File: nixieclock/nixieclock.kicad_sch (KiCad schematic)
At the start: 0 parts

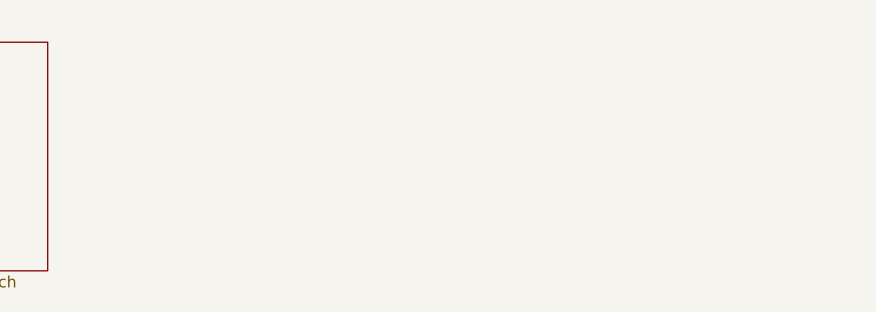
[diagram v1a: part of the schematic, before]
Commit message: added nixie breakout, began shift registers
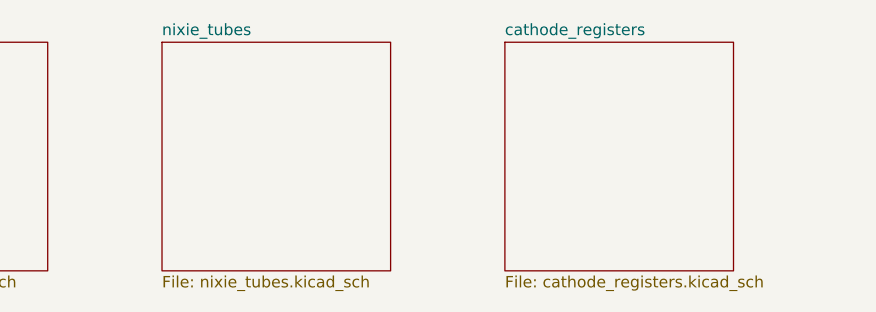
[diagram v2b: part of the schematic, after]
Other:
- added sheet cathode_registers (cathode_registers.kicad_sch)
- added sheet nixie_tubes (nixie_tubes.kicad_sch)
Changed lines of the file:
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@@
 (kicad_sch (version 20200828) (generator eeschema)
-  (page 1 2)
+  (page 1 4)
   (paper "A4")
   (title_block
     (title "Nixie Clock")
-    (date "2021-03-08")
+    (date "2021-03-10")
     (company "Bastian de Byl")
+  )
+  (sheet (at 101.6 25.4) (size 25.4 25.4)
+    (stroke (width 0.001) (type solid) (color 132 0 132 1))
+    (fill (color 255 255 255 0.0000))
+    (property "Sheet name" "cathode_registers" (id 0) (at 101.6 24.7641 0)
+      (effects (font (size 1.27 1.27)) (justify left bottom))
+    )
+    (property "Sheet file" "cathode_registers.kicad_sch" (id 1) (at 101.6 51.3089 0)
+      (effects (font (size 1.27 1.27)) (justify left top))
+    )
   )
   (sheet (at 25.4 25.4) (size 25.4 25.4)
@@
     )
     (property "Sheet file" "hv_supply.kicad_sch" (id 1) (at 25.4 51.3089 0)
+      (effects (font (size 1.27 1.27)) (justify left top))
+    )
+  )
+  (sheet (at 63.5 25.4) (size 25.4 25.4)
+    (stroke (width 0.001) (type solid) (color 132 0 132 1))
+    (fill (color 255 255 255 0.0000))
+    (property "Sheet name" "nixie_tubes" (id 0) (at 63.5 24.7641 0)
+      (effects (font (size 1.27 1.27)) (justify left bottom))
+    )
+    (property "Sheet file" "nixie_tubes.kicad_sch" (id 1) (at 63.5 51.3089 0)
       (effects (font (size 1.27 1.27)) (justify left top))
     )
@@
       (reference "U1") (unit 1) (value "LT3757AEMSE") (footprint "Package_SO:MSOP-10-1EP_3x3mm_P0.5mm_EP1.68x1.88mm")
     )
+    (path "/a46896f1-3299-462b-8eac-566ddac50b81/c7103b38-a6f4-42d2-a022-37c0fb310621"
+      (reference "R9") (unit 1) (value "R") (footprint "Resistor_SMD:R_0805_2012Metric_Pad1.15x1.40mm_HandSolder")
+    )
+    (path "/a46896f1-3299-462b-8eac-566ddac50b81/962332e7-a564-4eee-ba04-af4a2363d1a7"
+      (reference "R10") (unit 1) (value "R") (footprint "Resistor_SMD:R_0805_2012Metric_Pad1.15x1.40mm_HandSolder")
+    )
+    (path "/a46896f1-3299-462b-8eac-566ddac50b81/3cb47c1b-a308-4405-ab12-750a289a57fe"
+      (reference "R11") (unit 1) (value "R") (footprint "Resistor_SMD:R_0805_2012Metric_Pad1.15x1.40mm_HandSolder")
+    )
+    (path "/a46896f1-3299-462b-8eac-566ddac50b81/31d7a4f6-bd29-4607-8fc2-1aea2457c99a"
+      (reference "R12") (unit 1) (value "R") (footprint "Resistor_SMD:R_0805_2012Metric_Pad1.15x1.40mm_HandSolder")
+    )
+    (path "/a46896f1-3299-462b-8eac-566ddac50b81/55bc21e7-2697-464a-a01c-38e1e7b3f773"
+      (reference "R13") (unit 1) (value "R") (footprint "Resistor_SMD:R_0805_2012Metric_Pad1.15x1.40mm_HandSolder")
+    )
+    (path "/a46896f1-3299-462b-8eac-566ddac50b81/c23b582a-658a-4b65-9c96-b9e08b0bf0cc"
+      (reference "R14") (unit 1) (value "R") (footprint "Resistor_SMD:R_0805_2012Metric_Pad1.15x1.40mm_HandSolder")
+    )
+    (path "/a46896f1-3299-462b-8eac-566ddac50b81/6646077f-40fe-40f4-8bd0-e02e416e0ae9"
+      (reference "R15") (unit 1) (value "R") (footprint "Resistor_SMD:R_0805_2012Metric_Pad1.15x1.40mm_HandSolder")
+    )
+    (path "/a46896f1-3299-462b-8eac-566ddac50b81/0d7d00ef-2736-4754-8911-b0ba309be9da"
+      (reference "R16") (unit 1) (value "R") (footprint "Resistor_SMD:R_0805_2012Metric_Pad1.15x1.40mm_HandSolder")
+    )
+    (path "/a46896f1-3299-462b-8eac-566ddac50b81/ec2d7750-4711-4633-ae51-cab52b1fb7c7"
+      (reference "R17") (unit 1) (value "R") (footprint "Resistor_SMD:R_0805_2012Metric_Pad1.15x1.40mm_HandSolder")
+    )
+    (path "/a46896f1-3299-462b-8eac-566ddac50b81/d62867db-ccaa-4e9e-b09a-9c26817199fe"
+      (reference "R18") (unit 1) (value "R") (footprint "Resistor_SMD:R_0805_2012Metric_Pad1.15x1.40mm_HandSolder")
+    )
+    (path "/a46896f1-3299-462b-8eac-566ddac50b81/6ad2622d-22ff-4543-871a-5f06ac0a45ed"
+      (reference "R19") (unit 1) (value "R") (footprint "Resistor_SMD:R_0805_2012Metric_Pad1.15x1.40mm_HandSolder")
+    )
+    (path "/a46896f1-3299-462b-8eac-566ddac50b81/569c3ecb-8ab4-4304-b394-f90324cffda1"
+      (reference "R20") (unit 1) (value "R") (footprint "Resistor_SMD:R_0805_2012Metric_Pad1.15x1.40mm_HandSolder")
+    )
+    (path "/a46896f1-3299-462b-8eac-566ddac50b81/eaafd802-a0aa-46f0-beb4-15c99f9627aa"
+      (reference "V1") (unit 1) (value "IN14") (footprint "Personal:IN-14")
+    )
+    (path "/a46896f1-3299-462b-8eac-566ddac50b81/30cb2f61-bf62-4cf9-add2-c09f42e6b1ea"
+      (reference "V2") (unit 1) (value "IN14") (footprint "Personal:IN-14")
+    )
+    (path "/a46896f1-3299-462b-8eac-566ddac50b81/5064cf25-6e76-4e94-8248-7cc6b91daf3b"
+      (reference "V3") (unit 1) (value "IN14") (footprint "Personal:IN-14")
+    )
+    (path "/a46896f1-3299-462b-8eac-566ddac50b81/d99c5752-7e4c-4b30-a4f7-de6bf7e6014c"
+      (reference "V4") (unit 1) (value "IN14") (footprint "Personal:IN-14")
+    )
+    (path "/a645acc1-af0d-43da-834c-14426116caab/6ace0fd9-54a1-49a3-9e9d-846aed7512d7"
+      (reference "#PWR?") (unit 1) (value "GND") (footprint "")
+    )
+    (path "/a645acc1-af0d-43da-834c-14426116caab/de472645-4a4e-474d-9f12-cae105f2bbe0"
+      (reference "U?") (unit 1) (value "HV5522") (footprint "")
+    )
   )

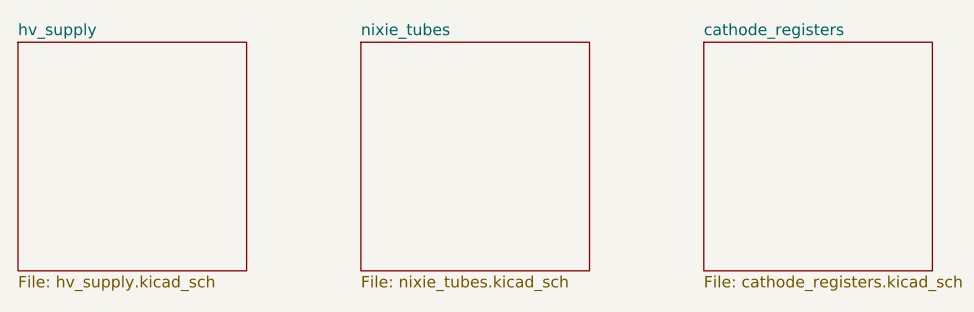
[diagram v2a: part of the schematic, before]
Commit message: finalized power supplies, most footprints, nixie breakout
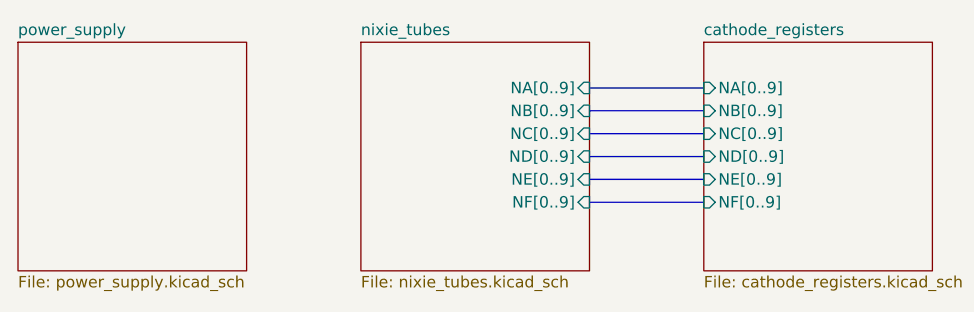
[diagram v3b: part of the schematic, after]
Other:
- sheet hv_supply renamed power_supply
- sheet cathode_registers ports: added NA[0..9], NB[0..9], NC[0..9], ND[0..9], NE[0..9], NF[0..9]; removed none
- sheet nixie_tubes ports: added NA[0..9], NB[0..9], NC[0..9], ND[0..9], NE[0..9], NF[0..9]; removed none
- sheet power_supply: file hv_supply.kicad_sch -> power_supply.kicad_sch

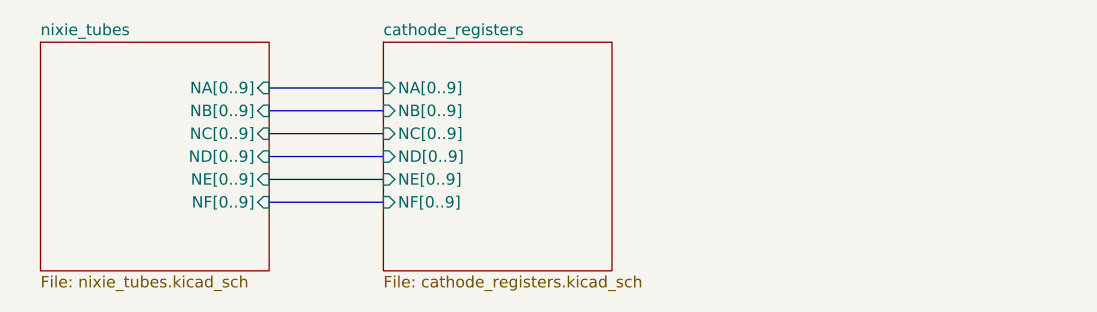
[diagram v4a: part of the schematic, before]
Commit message: began routing PCB, finalized registers design
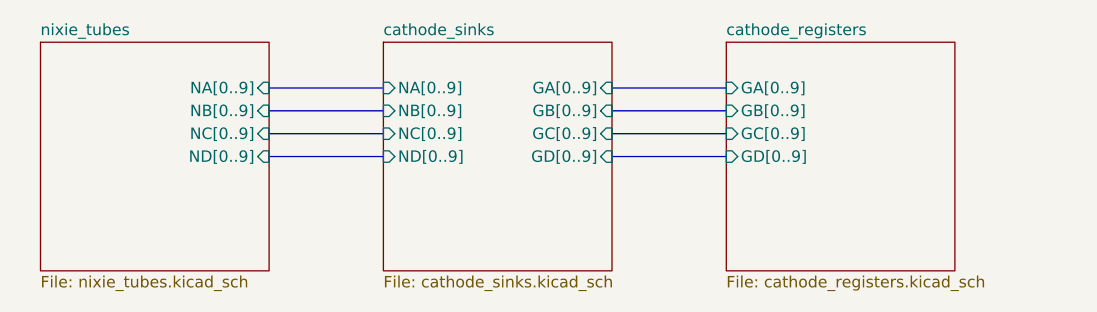
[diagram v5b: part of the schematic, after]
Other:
- added sheet cathode_sinks (cathode_sinks.kicad_sch)
- sheet cathode_registers ports: added GA[0..9], GB[0..9], GC[0..9], GD[0..9]; removed NA[0..9], NB[0..9], NC[0..9], ND[0..9], NE[0..9], NF[0..9]
- sheet nixie_tubes ports: added none; removed NE[0..9], NF[0..9]
- company: Bastian de Byl -> (none)

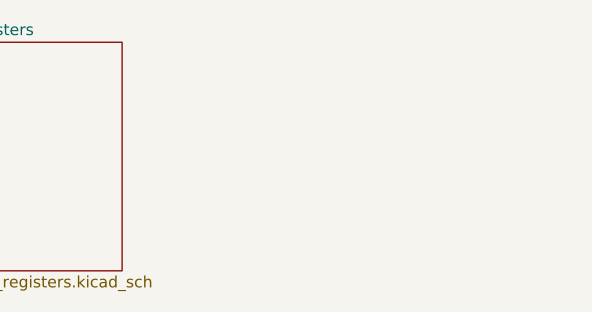
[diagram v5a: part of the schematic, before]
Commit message: began work on microcontroller (stm32f0)
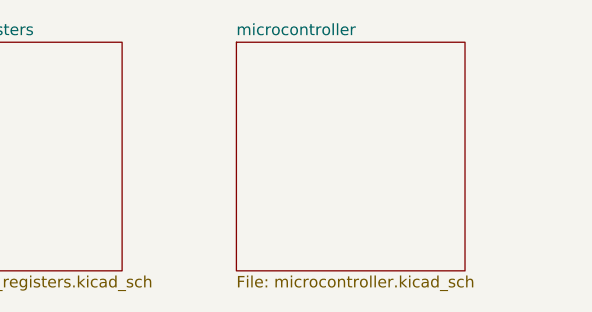
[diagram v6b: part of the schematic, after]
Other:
- added sheet microcontroller (microcontroller.kicad_sch)
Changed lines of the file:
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@@
+    )
+  )
+  (sheet (at 177.8 25.4) (size 25.4 25.4)
+    (stroke (width 0.0006) (type solid) (color 132 0 132 1))
+    (fill (color 255 255 255 0.0000))
+    (property "Sheet name" "microcontroller" (id 0) (at 177.8 24.7643 0)
+      (effects (font (size 1.27 1.27)) (justify left bottom))
+    )
+    (property "Sheet file" "microcontroller.kicad_sch" (id 1) (at 177.8 51.3087 0)
+      (effects (font (size 1.27 1.27)) (justify left top))
     )
   )
@@
     (path "/45da1564-3080-439e-9487-27ba0f449a7b/" (page "4"))
     (path "/a645acc1-af0d-43da-834c-14426116caab/" (page "5"))
+    (path "/a724e452-8dc5-4051-8b81-2fd3eafcc3bd/" (page "6"))
   )
   (symbol_instances
@@
       (reference "U7") (unit 1) (value "74HC595") (footprint "Package_SO:SOIC-16_4.55x10.3mm_P1.27mm")
     )
+    (path "/a724e452-8dc5-4051-8b81-2fd3eafcc3bd/1e6fa702-a73d-4c8c-abc8-db0dc159d5d3"
+      (reference "U8") (unit 1) (value "STM32F058R8Tx") (footprint "Package_QFP:LQFP-64_10x10mm_P0.5mm")
+    )
   )

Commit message: mostly finalized pcb layout, silkscreen graphics, etc
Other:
- sheet cathode_registers ports: added CLK, D, LCLK, ~OE, ~RES; removed none
- sheet microcontroller ports: added CLK, D, LCLK, ~OE, ~RES, ~SHDN; removed none
- sheet power_supply ports: added ~SHDN; removed none
- company: (none) -> Bastian de Byl

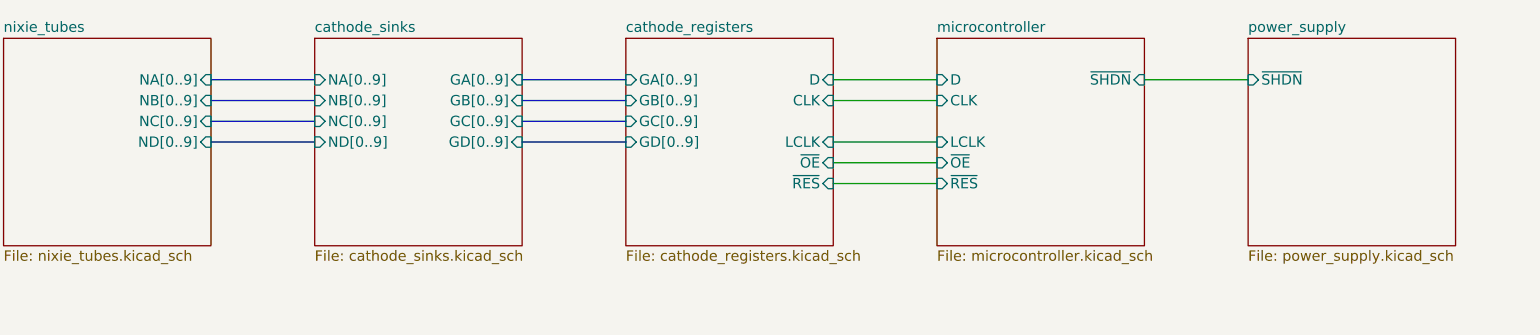
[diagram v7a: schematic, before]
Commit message: finalized neon bulb design (todo: pcb jumpers)
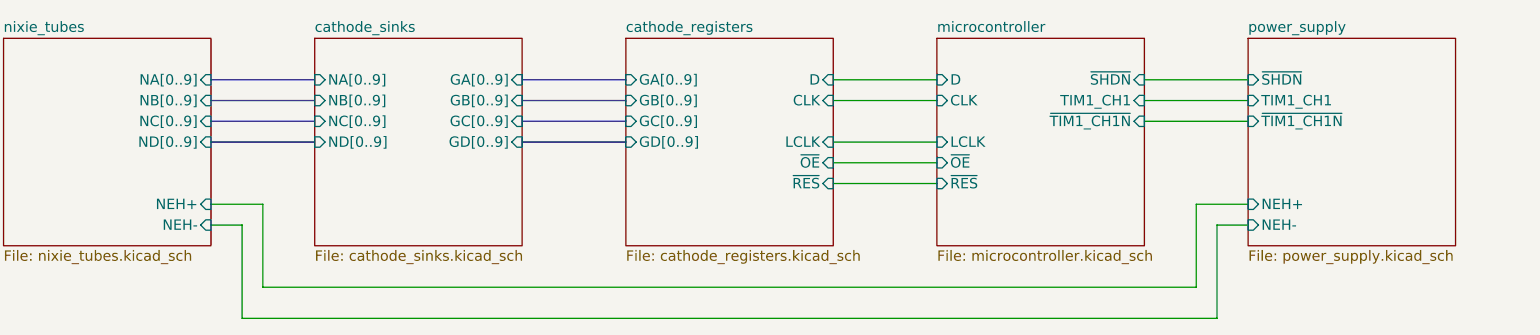
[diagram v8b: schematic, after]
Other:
- sheet microcontroller ports: added TIM1_CH1, ~TIM1_CH1N; removed none
- sheet nixie_tubes ports: added NEH+, NEH-; removed none
- sheet power_supply ports: added NEH+, NEH-, TIM1_CH1, ~TIM1_CH1N; removed none
